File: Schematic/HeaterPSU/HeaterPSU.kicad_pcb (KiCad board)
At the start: 2 copper layers, 100 x 35 mm, 56 parts, among them J1 SMPS2_SEC, J2 Heater Output, J3 Heater Control, J4 MCU_Interface, J5 High voltage warning, K1 Relay_TE_OJT_SH_124DM, Q1 IRF4905, Q2 BSS138, SW1 SW_Rotary_1P5T_ALPSALPINE_SRBV, U1 TPS54302, U2 TLP185, U3 TLP185

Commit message: First draft
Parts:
- moved R5 11.8 mm to (90.8, 76.1)
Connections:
- RV1 pad 1: GNDPWR -> Net-(R10-Pad2)
- RV1 pad 3: Net-(R10-Pad2) -> GNDPWR
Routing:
- net HeaterSense1: track 26.9 -> 18.3 mm
- net Net-(R10-Pad2): track 7.67 -> 12.7 mm
- net HeaterSense2: track 93.0 -> 93.8 mm
- net GNDPWR: vias 57 -> 59

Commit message: Minor layout changes
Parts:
- added G***: LOGO, Graphics:retronics_logo_24mm, B.Cu at (111.1, 73.5)
- moved D1 4.90 mm to (82.2, 65.5), turned to -90 degrees
- moved R3 2.69 mm to (84.7, 65.5)
- turned D3 to -90 degrees
- turned D5 to -90 degrees
- turned D6 to -90 degrees
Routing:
- net Net-(D5-Pad2): track 25.0 -> 15.6 mm
- net Net-(D6-Pad1): track 22.4 -> 17.4 mm
- net VDC: track 102.7 -> 107.5 mm, vias 3 -> 4
- net Net-(D6-Pad2): track 12.9 -> 9.03 mm
- net GNDPWR: track 18.5 -> 17.1 mm, vias 59 -> 56
- net Net-(D2-Pad1): track 8.19 -> 9.56 mm
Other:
- board text added: "."
- board text added: "JLCJLCJLCJLC"
- board text added: "µTracer Heater PSU 22_43_0119 Bjørner Sandom"

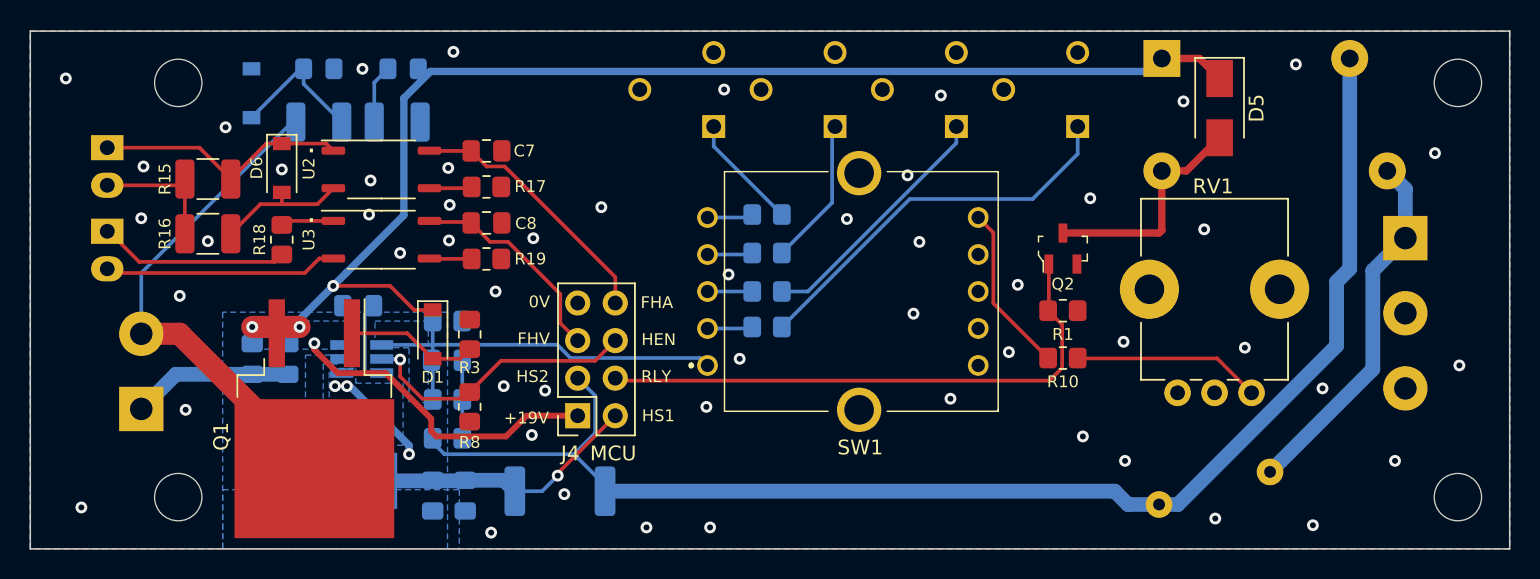
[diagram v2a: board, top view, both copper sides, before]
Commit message: Added load resistor, updated annotation, changed NTC footprint
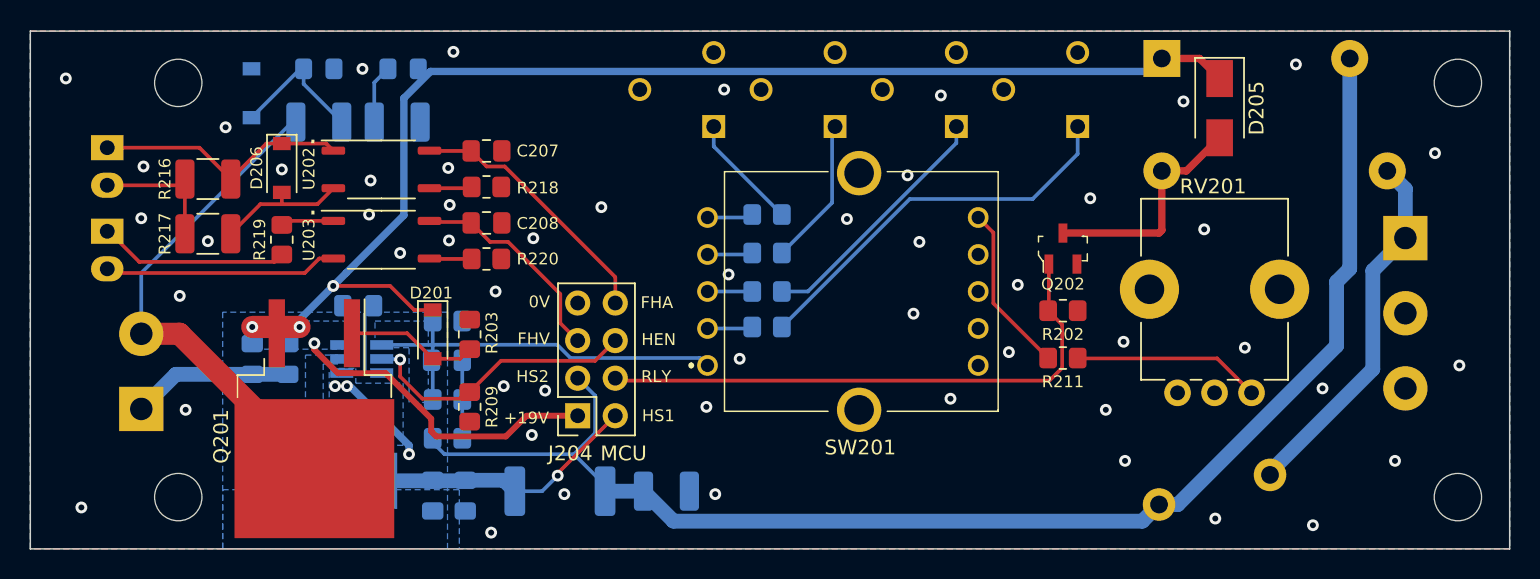
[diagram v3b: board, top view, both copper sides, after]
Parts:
- added R206: 3.9kΩ 1/2W, Resistor_SMD:R_1210_3225Metric_Pad1.30x2.65mm_HandSolder, B.Cu at (98.0, 76.1)
- L201: renamed from L1; value 10µH 6.7A -> 10µH 5.7A
- TH201: renamed from TH1; footprint Varistor:RV_Disc_D15.5mm_W5mm_P7.5mm -> myDevices:RV_Disc_D15.5mm_W4.5mm_P7.5mm
- renumbered C1 to C201, C2 to C202, C3 to C203, C4 to C204, C5 to C205, C6 to C206, C7 to C207, C8 to C208, D1 to D201, D4 to D202, D2 to D203, D3 to D204, D5 to D205, D6 to D206, H1 to H201, H2 to H202, H3 to H203, H4 to H204, J1 to J201, J2 to J202, J3 to J203, J4 to J204, J5 to J205, K1 to K201, Q1 to Q201, Q2 to Q202, R2 to R201, R1 to R202, R3 to R203, R4 to R204, R5 to R205, R6 to R207, R7 to R208, R8 to R209, R9 to R210, R10 to R211, R11 to R212, R12 to R213, R13 to R214, R14 to R215, R15 to R216, R16 to R217, R17 to R218, R18 to R219, R19 to R220, RV1 to RV201, RV2 to RV202, RV3 to RV203, RV4 to RV204, RV5 to RV205, SW1 to SW201, U1 to U201, U2 to U202, U3 to U203
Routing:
- net HeaterSense2: track 93.8 -> 94.7 mm
- net GNDPWR: vias 56 -> 55
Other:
- board text added: "µTracer Heater PSU 22_43_0119B Bjørner Sandom"
- board text removed: "µTracer Heater PSU 22_43_0119 Bjørner Sandom"

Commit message: Changed inductor footprint
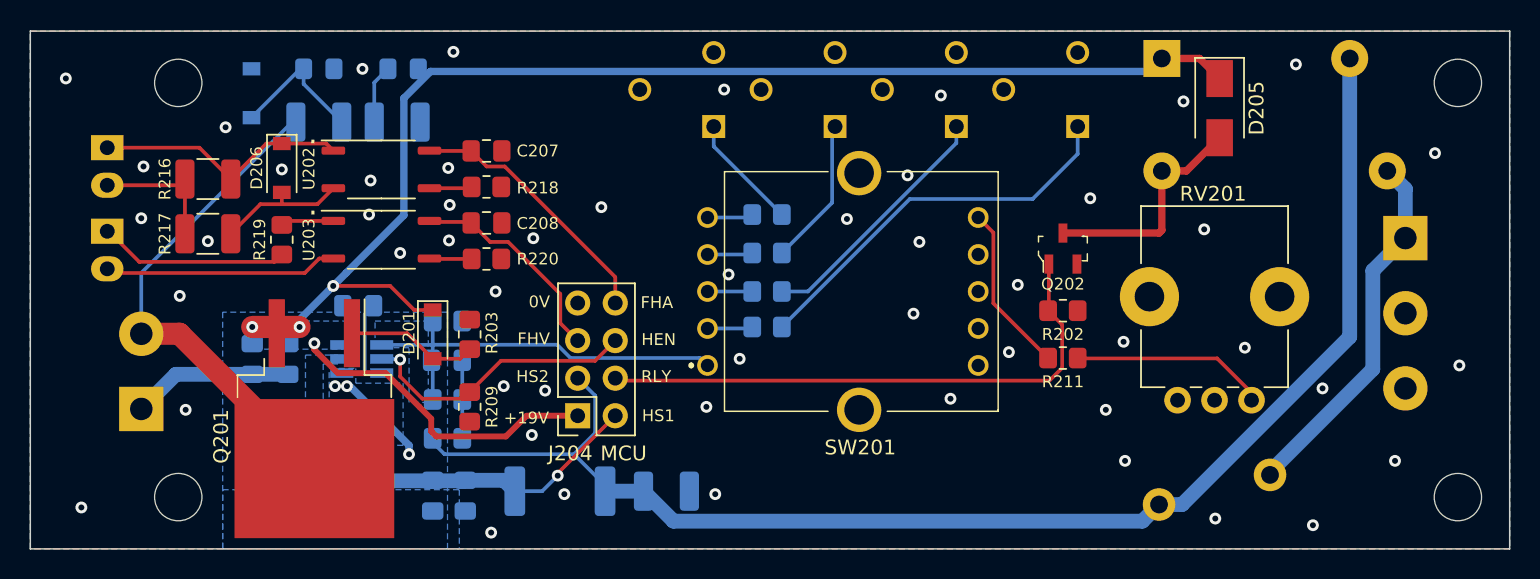
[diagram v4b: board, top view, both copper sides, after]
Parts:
- L201: value 10µH 5.7A -> 10µH 3.3A; footprint myDevices:L_8.5x8_H5.4_HandSolder -> Inductor_SMD:L_Taiyo-Yuden_NR-60xx_HandSoldering
- moved L201 3.93 mm to (74.0, 74.0)
- moved RV201 0.50 mm to (137.6, 70.0)
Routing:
- net HeaterSense1: track 18.3 -> 20.9 mm
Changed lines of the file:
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@@
   )
   (footprint "Potentiometer_THT:Potentiometer_Bourns_PTV09A-1_Single_Vertical" (layer "F.Cu")
-    (at 137.55 69.45 90)
+    (at 137.55 69.95 90)
     (descr "Potentiometer, vertical, Bourns PTV09A-1 Single, http://www.bourns.com/docs/Product-Datasheets/ptv09.pdf")
     (tags "Potentiometer vertical Bourns PTV09A-1 Single")
@@
     (property "Sheetname" "")
     (attr smd)
-    (fp_text reference "D201" (at -2.8 0.1) (layer "F.SilkS")
+    (fp_text reference "D201" (at -0.1 1.6 90) (layer "F.SilkS")
       (effects (font (size 0.8 0.8) (thickness 0.1)))
     )
@@
     )
   )
-  (footprint "myDevices:L_8.5x8_H5.4_HandSolder" (layer "B.Cu")
-    (at 70.3 75.4)
-    (descr "Choke, SMD, 7.3x7.3mm 3.5mm height")
-    (tags "Choke SMD")
-    (property "Sheetfile" "HeaterPSU.kicad_sch")
-    (property "Sheetname" "")
-    (attr smd)
-    (fp_text reference "L201" (at 4.05 -4.65 180) (layer "B.SilkS")
-      (effects (font (size 1 1) (thickness 0.15)) (justify mirror))
-    )
-    (fp_text value "10µH 5.7A" (at 4.3688 -5.1308) (layer "B.Fab")
-      (effects (font (size 1 1) (thickness 0.15)) (justify mirror))
-    )
-    (fp_text user "${REFERENCE}" (at 3.158 0) (layer "B.Fab")
-      (effects (font (size 1 1) (thickness 0.15)) (justify mirror))
-    )
-    (fp_line (start -0.542 2) (end -0.542 4) (layer "B.SilkS") (width 0.12))
-    (fp_line (start 9 -4) (end -0.542 -4) (layer "B.SilkS") (width 0.12))
-    (fp_line (start -0.542 -3.9972) (end -0.542 -1.9972) (layer "B.SilkS") (width 0.12))
-    (fp_line (start 9 -3.9972) (end 9 -1.9972) (layer "B.SilkS") (width 0.12))
-    (fp_line (start 9 2) (end 9 4) (layer "B.SilkS") (width 0.12))
-    (fp_line (start -0.542 4) (end 9 4) (layer "B.SilkS") (width 0.12))
-    (fp_line (start 9.5504 -4.1) (end 9.5504 4.1) (layer "B.CrtYd") (width 0.05))
-    (fp_line (start 9.5504 4.1) (end -1.042 4.1) (layer "B.CrtYd") (width 0.05))
-    (fp_line (start -1.042 4.1) (end -1.042 -4.1) (layer "B.CrtYd") (width 0.05))
-    (fp_line (start -1.042 -4.1) (end 9.5504 -4.1) (layer "B.CrtYd") (width 0.05))
-    (fp_line (start 8.89 3.9) (end 8.89 1.9812) (layer "B.Fab") (width 0.1))
-    (fp_line (start 8.9 -3.9) (end -0.492 -3.9) (layer "B.Fab") (width 0.1))
-    (fp_line (start -0.492 3.9) (end 8.9 3.9) (layer "B.Fab") (width 0.1))
-    (fp_line (start 8.9 -1.9812) (end 8.9 -3.9) (layer "B.Fab") (width 0.1))
-    (fp_line (start -0.492 3.9) (end -0.492 1.9812) (layer "B.Fab") (width 0.1))
-    (fp_line (start -0.482 -1.9812) (end -0.482 -3.9) (layer "B.Fab") (width 0.1))
-    (pad "1" smd rect (at 0 0) (size 2 3.8) (layers "B.Cu" "B.Paste" "B.Mask")
+  (footprint "Inductor_SMD:L_Taiyo-Yuden_NR-60xx_HandSoldering" (layer "B.Cu")
+    (at 73.975 74)
+    (descr "Inductor, Taiyo Yuden, NR series, Taiyo-Yuden_NR-60xx, 6.0mmx6.0mm")
+    (tags "inductor taiyo-yuden nr smd")
+    (property "Sheetfile" "HeaterPSU.kicad_sch")
+    (property "Sheetname" "")
+    (attr smd)
+    (fp_text reference "L201" (at 0 4 180) (layer "B.SilkS")
+      (effects (font (size 0.8 0.8) (thickness 0.1)) (justify mirror))
+    )
+    (fp_text value "10µH 3.3A" (at 0 -4.5 180) (layer "B.Fab")
+      (effects (font (size 1 1) (thickness 0.15)) (justify mirror))
+    )
+    (fp_text user "${REFERENCE}" (at 0 0 180) (layer "B.Fab")
+      (effects (font (size 1 1) (thickness 0.15)) (justify mirror))
+    )
+    (fp_line (start -4 3.1) (end 4 3.1) (layer "B.SilkS") (width 0.12))
+    (fp_line (start -4 -3.1) (end 4 -3.1) (layer "B.SilkS") (width 0.12))
+    (fp_line (start -4.25 3.25) (end -4.25 -3.25) (layer "B.CrtYd") (width 0.05))
+    (fp_line (start 4.25 -3.25) (end 4.25 3.25) (layer "B.CrtYd") (width 0.05))
+    (fp_line (start 4.25 3.25) (end -4.25 3.25) (layer "B.CrtYd") (width 0.05))
+    (fp_line (start -4.25 -3.25) (end 4.25 -3.25) (layer "B.CrtYd") (width 0.05))
+    (fp_line (start 2 -3) (end 0 -3) (layer "B.Fab") (width 0.1))
+    (fp_line (start 2 3) (end 0 3) (layer "B.Fab") (width 0.1))
+    (fp_line (start -3 2) (end -2 3) (layer "B.Fab") (width 0.1))
+    (fp_line (start -3 0) (end -3 2) (layer "B.Fab") (width 0.1))
+    (fp_line (start -3 -2) (end -2 -3) (layer "B.Fab") (width 0.1))
+    (fp_line (start 3 0) (end 3 2) (layer "B.Fab") (width 0.1))
+    (fp_line (start -2 3) (end 0 3) (layer "B.Fab") (width 0.1))
+    (fp_line (start -2 -3) (end 0 -3) (layer "B.Fab") (width 0.1))
+    (fp_line (start 3 0) (end 3 -2) (layer "B.Fab") (width 0.1))
+    (fp_line (start -3 0) (end -3 -2) (layer "B.Fab") (width 0.1))
+    (fp_line (start 3 2) (end 2 3) (layer "B.Fab") (width 0.1))
+    (fp_line (start 3 -2) (end 2 -3) (layer "B.Fab") (width 0.1))
+    (pad "1" smd rect (at -2.775 0) (size 2.45 5.9) (layers "B.Cu" "B.Paste" "B.Mask")
       (net 1 "Net-(C201-Pad1)") (pinfunction "1") (pintype "passive"))
-    (pad "2" smd rect (at 8.5 0) (size 2 3.8) (layers "B.Cu" "B.Paste" "B.Mask")
+    (pad "2" smd rect (at 2.775 0) (size 2.45 5.9) (layers "B.Cu" "B.Paste" "B.Mask")
       (net 9 "HeaterSense1") (pinfunction "2") (pintype "passive"))
-    (model "${KISYS3DMOD}/Inductor_SMD.3dshapes/L_7.3x7.3_H3.5.wrl"
+    (model "${KICAD6_3DMODEL_DIR}/Inductor_SMD.3dshapes/L_Taiyo-Yuden_NR-60xx.wrl"
       (offset (xyz 0 0 0))
       (scale (xyz 1 1 1))
@@
   (segment (start 84.7 66.5) (end 84.05 67.15) (width 0.25) (layer "F.Cu") (net 7))
   (segment (start 82.2 72.526) (end 82.2 72.8) (width 0.25) (layer "B.Cu") (net 8))
-  (segment (start 143.3 61.95) (end 143.3 66.272792) (width 1) (layer "B.Cu") (net 8))
   (segment (start 82.2 72.8) (end 83 73.6) (width 0.25) (layer "B.Cu") (net 8))
   (segment (start 130.175 78.125) (end 131.3 77) (width 1) (layer "B.Cu") (net 8))
   (segment (start 91.75 73.6) (end 93.175 72.175) (width 0.25) (layer "B.Cu") (net 8))
+  (segment (start 132.855634 77) (end 144.187719 65.667915) (width 1) (layer "B.Cu") (net 8))
   (segment (start 93.175 72.175) (end 93.175 69.635) (width 0.25) (layer "B.Cu") (net 8))
   (segment (start 93.85 75.7) (end 93.85 76.1) (width 0.25) (layer "B.Cu") (net 8))
+  (segment (start 144.187719 65.667915) (end 144.187719 46.85) (width 1) (layer "B.Cu") (net 8))
   (segment (start 93.175 69.635) (end 92 68.46) (width 0.25) (layer "B.Cu") (net 8))
-  (segment (start 144.187719 61.062281) (end 144.187719 46.85) (width 1) (layer "B.Cu") (net 8))
-  (segment (start 132.572792 77) (end 131.3 77) (width 1) (layer "B.Cu") (net 8))
   (segment (start 98.475 78.125) (end 130.175 78.125) (width 1) (layer "B.Cu") (net 8))
   (segment (start 83 73.6) (end 91.75 73.6) (width 0.25) (layer "B.Cu") (net 8))
-  (segment (start 143.3 66.272792) (end 132.572792 77) (width 1) (layer "B.Cu") (net 8))
   (segment (start 91.75 73.6) (end 93.85 75.7) (width 0.25) (layer "B.Cu") (net 8))
   (segment (start 96.45 76.1) (end 93.85 76.1) (width 1) (layer "B.Cu") (net 8))
-  (segment (start 143.3 61.95) (end 144.187719 61.062281) (width 1) (layer "B.Cu") (net 8))
+  (segment (start 131.3 77) (end 132.855634 77) (width 1) (layer "B.Cu") (net 8))
   (segment (start 96.45 76.1) (end 98.475 78.125) (width 1) (layer "B.Cu") (net 8))
   (segment (start 90.65 74.89) (end 94.54 71) (width 0.25) (layer "F.Cu") (net 9))
@@
   (via (at 90.65 75.05) (size 0.8) (drill 0.4) (layers "F.Cu" "B.Cu") (net 9))
   (segment (start 87.0125 75.3625) (end 87.75 76.1) (width 1) (layer "B.Cu") (net 9))
+  (segment (start 84.4 75.3625) (end 84.3625 75.4) (width 1) (layer "B.Cu") (net 9))
   (segment (start 87.75 76.1) (end 89.6 76.1) (width 0.25) (layer "B.Cu") (net 9))
-  (segment (start 84.3625 75.4) (end 84.4 75.3625) (width 1) (layer "B.Cu") (net 9))
+  (segment (start 84.3625 75.4) (end 78.15 75.4) (width 1) (layer "B.Cu") (net 9))
   (segment (start 84.4 75.3625) (end 87.0125 75.3625) (width 1) (layer "B.Cu") (net 9))
   (segment (start 89.6 76.1) (end 90.65 75.05) (width 0.25) (layer "B.Cu") (net 9))
-  (segment (start 78.8 75.4) (end 84.3625 75.4) (width 1) (layer "B.Cu") (net 9))
+  (segment (start 78.15 75.4) (end 76.75 74) (width 1) (layer "B.Cu") (net 9))
   (segment (start 78.25 48.475) (end 79.175 47.55) (width 0.25) (layer "B.Cu") (net 10))
   (segment (start 78.25 51.15) (end 78.25 48.475) (width 0.25) (layer "B.Cu") (net 10))

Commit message: MCU Board adapted for 3.3V operation
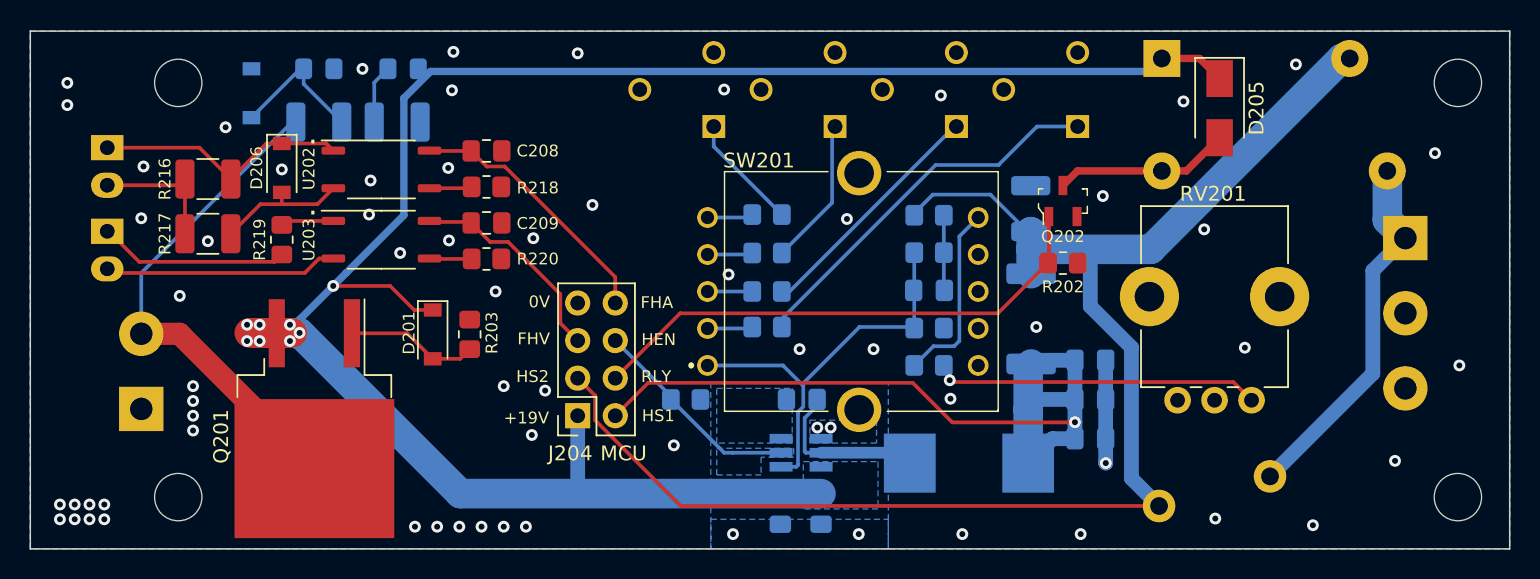
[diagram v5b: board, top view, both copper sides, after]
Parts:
- added C202: 22µF 25V, Capacitor_SMD:C_0805_2012Metric_Pad1.18x1.45mm_HandSolder, B.Cu at (126.7, 69.9)
- L201: value 10µH 3.3A -> 22µH 4.1A; footprint Inductor_SMD:L_Taiyo-Yuden_NR-60xx_HandSoldering -> Inductor_SMD:L_Wuerth_HCI-1040
- R209: moved to B.Cu
- R211: value 3.3kΩ -> 4.3kΩ; moved to B.Cu
- moved C204 45.4 mm to (126.7, 67.2), turned to 180 degrees
- moved L201 44.5 mm to (118.5, 74.2)
- moved C203 42.4 mm to (126.7, 72.5), turned to 180 degrees
- moved C206 37.4 mm to (108.5, 77.3)
- moved C205 37.1 mm to (105.7, 77.3)
- moved R206 35.9 mm to (115.8, 57.5)
- moved R208 34.0 mm to (115.8, 60.0)
- moved R205 33.9 mm to (122.7, 64.5), turned to 90 degrees
- moved C207 32.9 mm to (115.8, 62.5)
- moved R210 32.6 mm to (115.8, 65.1)
- moved R207 31.2 mm to (122.6, 57.0), turned to 90 degrees
- moved C201 30.6 mm to (107.2, 69.9), turned to 180 degrees
- moved U201 30.4 mm to (107.1, 73.5), turned to 180 degrees
- moved G*** 28.5 mm to (89.0, 55.5)
- moved R209 14.6 mm to (99.3, 69.9), turned to 180 degrees
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- renumbered C202 to C203, C203 to C204, C204 to C205, C205 to C206, C206 to C207, C207 to C208, C208 to C209, R207 to R206, R206 to R207
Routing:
- net HeaterSense1: track 20.9 -> 55.6 mm
- net VDC: track 107.5 -> 134.3 mm, vias 4 -> 8
- net GNDPWR: track 17.1 -> 6.96 mm, vias 55 -> 67
- net Net-(R211-Pad2): track 12.7 -> 22.1 mm, vias 0 -> 1
- net HeaterSense2: track 94.9 -> 102.6 mm
- net Net-(C201-Pad1): track 4.95 -> 11.3 mm
- net Net-(C201-Pad2): track 5.87 -> 0.00 mm
- net Heater_EN: track 19.2 -> 14.5 mm, vias 1 -> 0
- net Net-(D205-Pad2): track 15.6 -> 11.9 mm
- net RLY_CTRL: track 38.1 -> 35.7 mm
- net /VSEL_VAR: track 11.5 -> 12.6 mm
- net Net-(R215-Pad2): track 26.7 -> 25.9 mm
- net Net-(R214-Pad2): track 17.1 -> 16.4 mm
- added copper zone on B.Cu, net Heater_EN
- added copper zone on B.Cu, net Net-(C201-Pad2)
- removed copper zone on B.Cu, net /VSEL_COM
- removed copper zone on B.Cu, net Net-(C201-Pad1)
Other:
- board text added: "µTracer Heater PSU 22_43_0119C Bjørner Sandom"
- board text removed: "µTracer Heater PSU 22_43_0119B Bjørner Sandom"
